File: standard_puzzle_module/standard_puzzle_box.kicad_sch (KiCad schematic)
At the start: 27 parts, among them J1 Screw_Terminal_01x02, J2 Screw_Terminal_01x04, J4 Screw_Terminal_01x02, J5 Screw_Terminal_01x02, Q2 IRLZ44N, U1 ESP32-C3-DevKitM-1, U4 PC817, U5 TSR2-2450, U6 PC817

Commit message: chore: clean up
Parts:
- removed R10: 1k Ohm, symbol Device:R
- added C9: 10nF, symbol Device:C
- added D5, D6: 1N5711, Diode_THT:D_DO-35_SOD27_P7.62mm_Horizontal, symbol Diode:1N5711
- added J3: Screw_Terminal_01x04, symbol Connector:Screw_Terminal_01x04
- added R12: 4.7 kOhm, symbol Device:R
- added R13: 10k Ohm, symbol Device:R
- added R14: 100 kOhm, symbol Device:R
- D3: value PTVS5V0Z1USK -> PTVS3V3Z1USK
- R11: value 330 Ohm -> 100 Ohm
- R7: value 1k Ohm -> 3.3k Ohm
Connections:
- net GNDD is gone; now on net GND: C6.2, D3.2 (A), U4.3
- net +12V: now also F2.1, J1.1 (Pin_1), U6.4
- net +3.3V: now also U1.2 (3V3), U1.3 (3V3), D5.1 (K), J3.2 (Pin_2); no longer C6.1, R11.2, R8.2
- net +5V: now also J3.1 (Pin_1)
- net GND: now also U1.1 (GND), U1.12 (GND), U1.15 (GND), U1.16 (GND), U1.19 (GND), U1.24 (GND), U1.27 (GND), U1.30 (GND), U1.6 (GND), U1.8 (GND), C9.2, D6.2 (A), J3.4 (Pin_4), R13.1, R14.2; no longer U6.3
- net GPIO: now reaches R6.1, U4.4
- net GPIO: now also C6.1, R8.2, C9.1, D5.2 (A), D6.1 (K), R12.2, R14.1
- net at Q2.1 (G): now also U6.3, R13.2; no longer U6.4
- net at J2.3 (Pin_3), R11.1: now also D3.1 (K)
- net at C1.1, C2.1, D2.1 (K)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: no longer D4.1 (K)
- net at D2.2 (A), F2.2: now also D4.1 (K)
- new net: J3.3 (Pin_3), R12.1
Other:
- added sheet boolean_input (boolean_input.kicad_sch)
- added sheet boolean_output (boolean_output.kicad_sch)
- added sheet power_regulation (power_regulation.kicad_sch)
- added sheet signal_input (signal_input.kicad_sch)
- added sheet signal_output (signal_output.kicad_sch)
- note removed: "Buck converter (12V -> 5V, 2A)"
- note removed: "TVS Diode Transient Voltage Suppresion"
- title: (none) -> Standard puzzle module
- moved on the sheet: C1, C2, C3, C4, C6, D2, D3, D4, F2, J1, R6, U1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

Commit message: feat: unscrew git tracking
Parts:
- removed C1, C8: 477uF, symbol Device:C_Polarized
- removed C2, C4, C6, C7: 100nF, symbol Device:C
- removed C3: 47uF, symbol Device:C_Polarized
- removed C9: 10nF, symbol Device:C
- removed D1, D1flyback1: 1N4007, Diode_THT:D_DO-41_SOD81_P10.16mm_Horizontal, symbol Diode:1N4007
- removed D2: D_Schottky, symbol Device:D_Schottky
- removed D3: PTVS3V3Z1USK, Diode_SMD:Nexperia_DSN1608-2_1.6x0.8mm, symbol Diode:PTVS5V0Z1USK
- removed D4: PTVS15VZ1USK, Diode_SMD:Nexperia_DSN1608-2_1.6x0.8mm, symbol Diode:PTVS15VZ1USK
- removed D5, D6: 1N5711, Diode_THT:D_DO-35_SOD27_P7.62mm_Horizontal, symbol Diode:1N5711
- removed F2: Polyfuse 2A, symbol Device:Polyfuse
- removed J1, J4, J5: Screw_Terminal_01x02, symbol Connector:Screw_Terminal_01x02
- removed J2, J3: Screw_Terminal_01x04, symbol Connector:Screw_Terminal_01x04
- removed Q2: IRLZ44N, Package_TO_SOT_THT:TO-220-3_Vertical, symbol Transistor_FET:IRLZ44N
- removed R11: 100 Ohm, symbol Device:R
- removed R12: 4.7 kOhm, symbol Device:R
- removed R13: 10k Ohm, symbol Device:R
- removed R14: 100 kOhm, symbol Device:R
- removed R6: 10k, symbol Device:R
- removed R7: 3.3k Ohm, symbol Device:R
- removed R8: 330 Ohm, symbol Device:R
- removed U4, U6: PC817, Package_DIP:DIP-4_W7.62mm, symbol Isolator:PC817
- removed U5: TSR2-2450, Converter_DCDC:Converter_DCDC_TRACO_TSR2-xxxx_THT, symbol Converter_DCDC:TSR2-2450
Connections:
- net signal_input/signal_input: now also U1.9 (IO0)
- net signal_input1/signal_input: now reaches U1.10 (IO1)
- net boolean_output2/out: now reaches U1.11 (IO10)
- net signal_output1/out: now reaches U1.20 (IO4)
- net boolean_input1/in: now reaches U1.21 (IO5)
- net boolean_output/out: now reaches U1.22 (IO6)
- net boolean_input2/in: now reaches U1.23 (IO7)
- net boolean_input3/in: now reaches U1.25 (IO8)
- net boolean_output1/out: now reaches U1.26 (IO9)
- net boolean_input/in: now reaches U1.4 (IO2)
- net signal_output/out: now reaches U1.5 (IO3)
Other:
- added sheet boolean_input1 (boolean_input.kicad_sch)
- added sheet boolean_input2 (boolean_input.kicad_sch)
- added sheet boolean_input3 (boolean_input.kicad_sch)
- added sheet boolean_output1 (boolean_output.kicad_sch)
- added sheet boolean_output2 (boolean_output.kicad_sch)
- added sheet signal_input1 (signal_input.kicad_sch)
- added sheet signal_output1 (signal_output.kicad_sch)
- sheet boolean_input ports: added in; removed none
- sheet boolean_output ports: added out; removed none
- sheet signal_output ports: added out; removed none
- note added: "## About ESP32-C3 pins ### Boot pins GPIO 2, GPIO 8, GPIO 9 must be HIGH at boot / startup. Since the boolean blocks pull the pin up to 3.3V, they should be safe to use. If the pin is not populated, the pin is pulled up internally. ### ADC2 PIN GPIO 5 is reserved for WIFI (ADC2) and can't be used for signal sampling. Using it for boolean input or output should be fine. ### USB pins (GPIO18, GPIO1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"
- note added: "## Pin layout GPIO 0: signal_in GPIO 1: signal_in GPIO 2: bool_in GPIO 3: signal_out GPIO 4: signal_out GPIO 5: bool_in GPIO 6: bool_out GPIO 7: bool_in GPIO 8: bool_in GPIO 9: bool_out GPIO 10:bool_out"

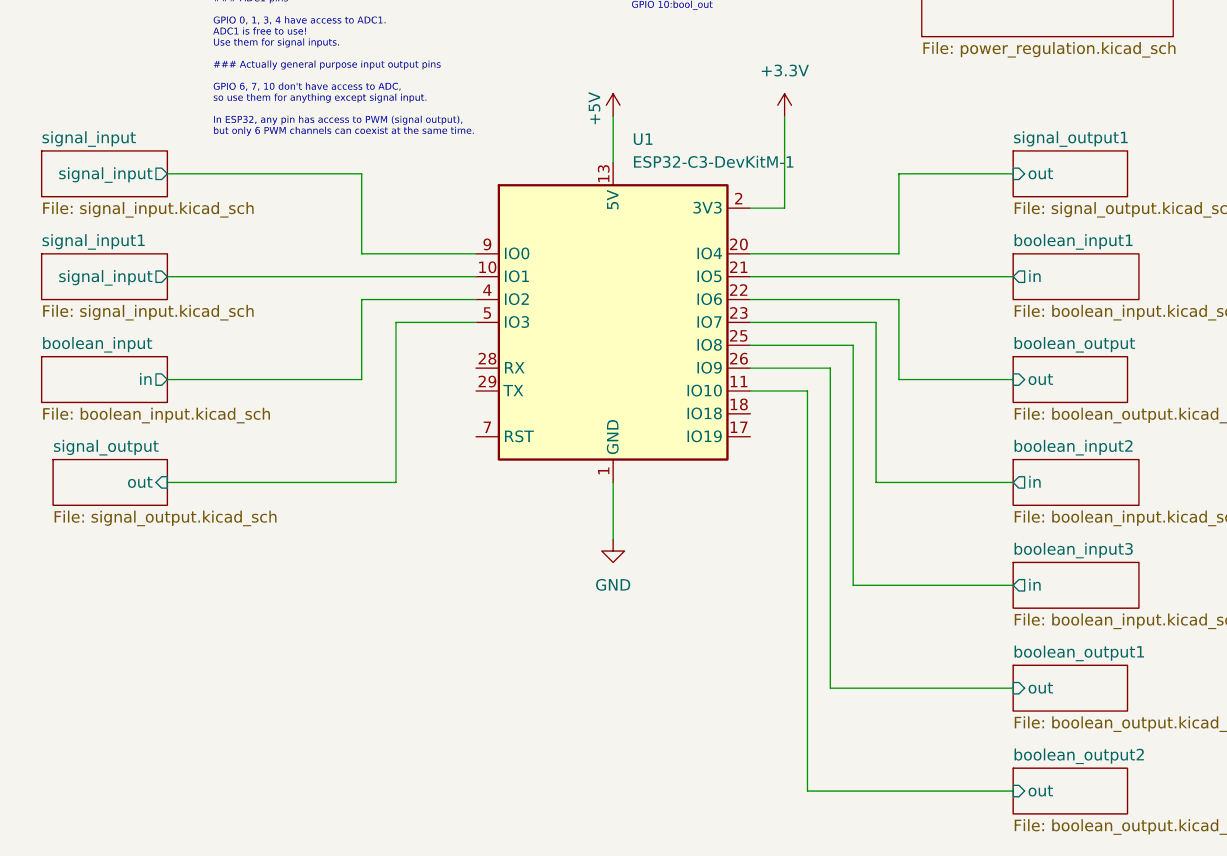
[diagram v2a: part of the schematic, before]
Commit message: feat: clean up schematic references and run clean annotation
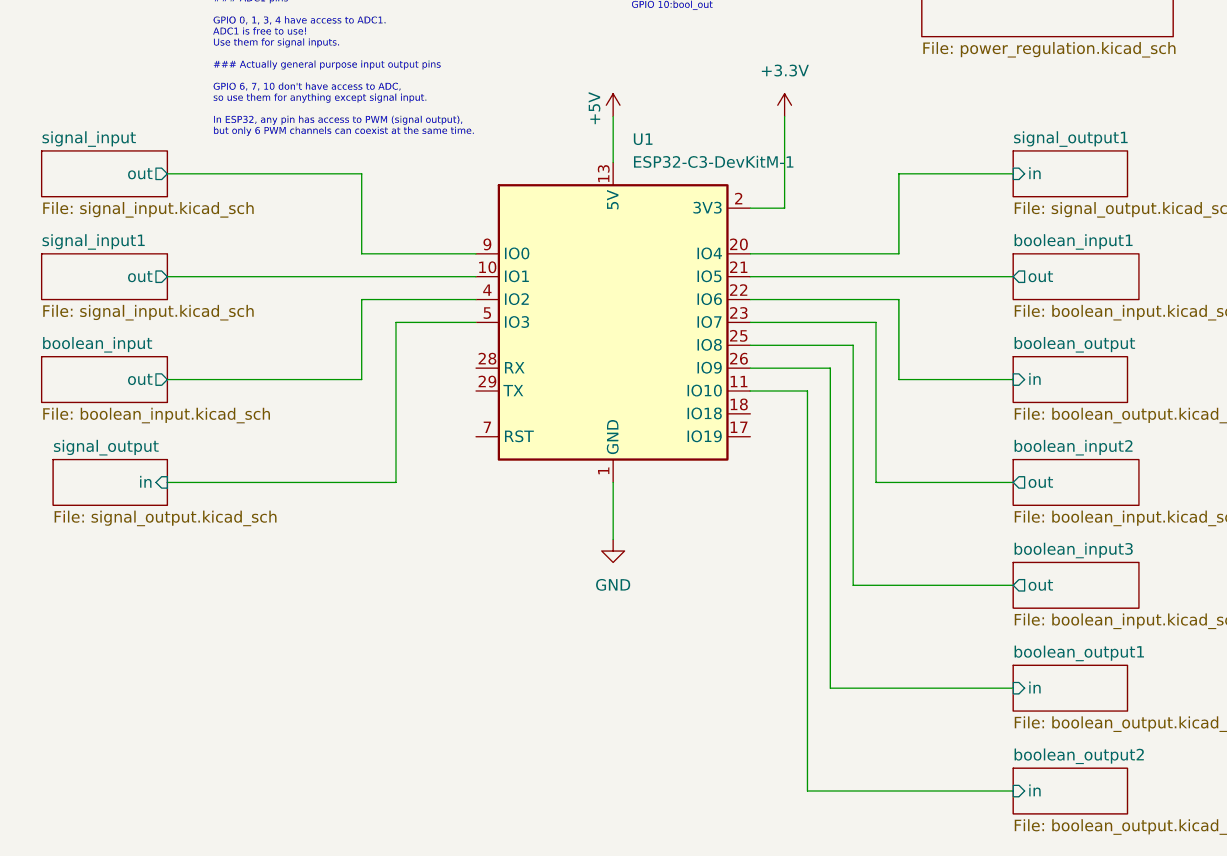
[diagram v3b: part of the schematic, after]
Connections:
- net boolean_input/in renamed boolean_input/out
- net boolean_input1/in renamed boolean_input1/out
- net boolean_input2/in renamed boolean_input2/out
- net boolean_input3/in renamed boolean_input3/out
- net boolean_output/out renamed boolean_output/in
- net boolean_output1/out renamed boolean_output1/in
- net boolean_output2/out renamed boolean_output2/in
- net signal_input/signal_input renamed signal_input/out
- net signal_input1/signal_input renamed signal_input1/out
- net signal_output/out renamed signal_output/in
- net signal_output1/out renamed signal_output1/in
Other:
- sheet boolean_input ports: added out; removed in
- sheet boolean_input1 ports: added out; removed in
- sheet boolean_input2 ports: added out; removed in
- sheet boolean_input3 ports: added out; removed in
- sheet boolean_output ports: added in; removed out
- sheet boolean_output1 ports: added in; removed out
- sheet boolean_output2 ports: added in; removed out
- sheet signal_input ports: added out; removed signal_input
- sheet signal_input1 ports: added out; removed signal_input
- sheet signal_output ports: added in; removed out
- sheet signal_output1 ports: added in; removed out

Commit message: feat: dump working files before blackout
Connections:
- no-connect marks 0 -> 5
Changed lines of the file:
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@@
 		)
+	)
+	(no_connect
+		(at 158.75 115.57)
+	)
+	(no_connect
+		(at 158.75 118.11)
+	)
+	(no_connect
+		(at 128.27 113.03)
+	)
+	(no_connect
+		(at 128.27 118.11)
+	)
+	(no_connect
+		(at 128.27 110.49)
 	)
 	(wire

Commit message: feat: salvaging stuff after lossy crash
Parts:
- removed U1: ESP32-C3-DevKitM-1, RF_Module:ESP32-C3-DevKitM-1, symbol RF_Module:ESP32-C3-DevKitM-1
- added U2: ESP32-C3-SuperMini, ESP32C3-SuperMini:ESP32-C3-SuperMini, symbol ESP32-C3-SuperMini:ESP32-C3-SuperMini
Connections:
- net +3.3V: now also U2. (3V3)
- net +5V: now also U2. (3V3)
- net GND: now also U2. (3V3)
- net boolean_input/out: now also U2.2 (GPIO2)
- net boolean_input1/out: now also U2.5 (GPIO5)
- net boolean_input2/out: now also U2.7 (GPIO7)
- net boolean_input3/out: now also U2.8 (GPIO8)
- net boolean_output/in: now also U2.6 (GPIO6)
- net boolean_output1/in: now also U2.9 (GPIO9)
- net boolean_output2/in: now also U2.10 (GPIO10)
- net signal_input/out: now also U2.0 (GPIO0)
- net signal_input1/out: now also U2.1 (GPIO1)
- net signal_output/in: now also U2.3 (GPIO3)
- net signal_output1/in: now also U2.4 (GPIO4)
- no-connect marks 5 -> 2

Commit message: feat: improve component placement for pcb
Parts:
- U1: renamed from U2; footprint ESP32C3-SuperMini:ESP32-C3-SuperMini -> ESP32-C3-SuperMini:ESP32-C3-SuperMini
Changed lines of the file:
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@@
 		(dnp no)
 		(fields_autoplaced yes)
-		(property "Reference" "U2"
+		(property "Reference" "U1"
 			(at 142.24 121.158 0)
 			(hide yes)
@@
 			)
 		)
-		(property "Footprint" "ESP32C3-SuperMini:ESP32-C3-SuperMini"
+		(property "Footprint" "ESP32-C3-SuperMini:ESP32-C3-SuperMini"
 			(at 142.24 104.14 0)
 			(hide yes)
@@
 			(project "standard_puzzle_box"
 				(path "/13314f97-080e-4924-a8fe-b4d224920625"
-					(reference "U2")
+					(reference "U1")
 					(unit 1)
 				)

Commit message: feat: DRC approved prototype of the board
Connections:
- net +3.3V: now also U1.3V3; no longer U1. (3V3)
- net +5V: now also U1.5V; no longer U1. (3V3)
- net GND: now also U1.GND; no longer U1. (3V3)
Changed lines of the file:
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@@
+	(wire
+		(pts
+			(xy 127 115.57) (xy 130.81 115.57)
+		)
+		(stroke
+			(width 0)
+			(type default)
+		)
+	)
 	(wire
 		(pts
@@
 	(wire
 		(pts
+			(xy 127 127) (xy 127 115.57)
+		)
+		(stroke
+			(width 0)
+			(type default)
+		)
+	)
+	(wire
+		(pts
 			(xy 166.37 115.57) (xy 166.37 148.59)
 		)
@@
 	(wire
 		(pts
-			(xy 125.73 115.57) (xy 130.81 115.57)
+			(xy 130.81 127) (xy 127 127)
 		)
 		(stroke
@@
 	(symbol
 		(lib_id "power:+5V")
-		(at 125.73 115.57 90)
+		(at 130.81 127 270)
 		(unit 1)
 		(body_style 1)
@@
 		(dnp no)
 		(property "Reference" "#PWR07"
-			(at 129.54 115.57 0)
+			(at 127 127 0)
 			(hide yes)
 			(show_name no)
@@
 		)
 		(property "Value" "+5V"
-			(at 128.27 114.3 90)
+			(at 128.27 128.27 90)
 			(show_name no)
 			(do_not_autoplace no)
@@
 		)
 		(property "Footprint" ""
-			(at 125.73 115.57 0)
+			(at 130.81 127 0)
 			(hide yes)
 			(show_name no)
@@
 		)
 		(property "Datasheet" ""
-			(at 125.73 115.57 0)
+			(at 130.81 127 0)
 			(hide yes)
 			(show_name no)
@@
 		)
 		(property "Description" "Power symbol creates a global label with name \"+5V\""
-			(at 125.73 115.57 0)
+			(at 130.81 127 0)
 			(hide yes)
 			(show_name no)
@@
 		(pin "0"
 		)
-		(pin ""
-		)
-		(pin ""
-		)
-		(pin ""
+		(pin "3V3"
+		)
+		(pin "5V"
+		)
+		(pin "GND"
 		)
 		(instances
